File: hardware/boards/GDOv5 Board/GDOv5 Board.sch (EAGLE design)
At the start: 27 parts, among them IC1 DS1820, IC2 3.3V REG, J1 DCJ0202, Q1 BSS84, Q2 BSS138, Q3 BSS138

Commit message: Finalized version of board for OshPark
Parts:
- Q2, Q3: device bss138_10:BSS138 -> Ava:BSS138
- R10, R9: value 50 -> 50Ω
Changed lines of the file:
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@@
 <grid distance="0.1" unitdist="inch" unit="inch" style="lines" multiple="1" display="no" altdistance="0.01" altunitdist="inch" altunit="inch"/>
 <layers>
-<layer number="1" name="Top" color="4" fill="1" visible="no" active="no"/>
-<layer number="16" name="Bottom" color="1" fill="1" visible="no" active="no"/>
-<layer number="17" name="Pads" color="2" fill="1" visible="no" active="no"/>
-<layer number="18" name="Vias" color="2" fill="1" visible="no" active="no"/>
-<layer number="19" name="Unrouted" color="6" fill="1" visible="no" active="no"/>
-<layer number="20" name="Dimension" color="15" fill="1" visible="no" active="no"/>
-<layer number="21" name="tPlace" color="7" fill="1" visible="no" active="no"/>
-<layer number="22" name="bPlace" color="7" fill="1" visible="no" active="no"/>
-<layer number="23" name="tOrigins" color="15" fill="1" visible="no" active="no"/>
-<layer number="24" name="bOrigins" color="15" fill="1" visible="no" active="no"/>
-<layer number="25" name="tNames" color="7" fill="1" visible="no" active="no"/>
-<layer number="26" name="bNames" color="7" fill="1" visible="no" active="no"/>
-<layer number="27" name="tValues" color="7" fill="1" visible="no" active="no"/>
-<layer number="28" name="bValues" color="7" fill="1" visible="no" active="no"/>
+<layer number="1" name="Top" color="4" fill="1" visible="yes" active="no"/>
+<layer number="16" name="Bottom" color="1" fill="1" visible="yes" active="no"/>
+<layer number="17" name="Pads" color="2" fill="1" visible="yes" active="no"/>
+<layer number="18" name="Vias" color="2" fill="1" visible="yes" active="no"/>
+<layer number="19" name="Unrouted" color="6" fill="1" visible="yes" active="no"/>
+<layer number="20" name="Dimension" color="15" fill="1" visible="yes" active="no"/>
+<layer number="21" name="tPlace" color="7" fill="1" visible="yes" active="no"/>
+<layer number="22" name="bPlace" color="7" fill="1" visible="yes" active="no"/>
+<layer number="23" name="tOrigins" color="15" fill="1" visible="yes" active="no"/>
+<layer number="24" name="bOrigins" color="15" fill="1" visible="yes" active="no"/>
+<layer number="25" name="tNames" color="7" fill="1" visible="yes" active="no"/>
+<layer number="26" name="bNames" color="7" fill="1" visible="yes" active="no"/>
+<layer number="27" name="tValues" color="7" fill="1" visible="yes" active="no"/>
+<layer number="28" name="bValues" color="7" fill="1" visible="yes" active="no"/>
 <layer number="29" name="tStop" color="7" fill="3" visible="no" active="no"/>
 <layer number="30" name="bStop" color="7" fill="6" visible="no" active="no"/>
@@
 <layer number="35" name="tGlue" color="7" fill="4" visible="no" active="no"/>
 <layer number="36" name="bGlue" color="7" fill="5" visible="no" active="no"/>
-<layer number="37" name="tTest" color="7" fill="1" visible="no" active="no"/>
-<layer number="38" name="bTest" color="7" fill="1" visible="no" active="no"/>
+<layer number="37" name="tTest" color="7" fill="1" visible="yes" active="no"/>
+<layer number="38" name="bTest" color="7" fill="1" visible="yes" active="no"/>
 <layer number="39" name="tKeepout" color="4" fill="11" visible="no" active="no"/>
 <layer number="40" name="bKeepout" color="1" fill="11" visible="no" active="no"/>
@@
 <layer number="44" name="Drills" color="7" fill="1" visible="no" active="no"/>
 <layer number="45" name="Holes" color="7" fill="1" visible="no" active="no"/>
-<layer number="46" name="Milling" color="3" fill="1" visible="no" active="no"/>
-<layer number="47" name="Measures" color="7" fill="1" visible="no" active="no"/>
-<layer number="48" name="Document" color="7" fill="1" visible="no" active="no"/>
-<layer number="49" name="Reference" color="7" fill="1" visible="no" active="no"/>
-<layer number="50" name="dxf" color="7" fill="1" visible="no" active="no"/>
-<layer number="51" name="tDocu" color="7" fill="1" visible="no" active="no"/>
-<layer number="52" name="bDocu" color="7" fill="1" visible="no" active="no"/>
-<layer number="53" name="tGND_GNDA" color="7" fill="9" visible="no" active="no"/>
-<layer number="54" name="bGND_GNDA" color="1" fill="9" visible="no" active="no"/>
-<layer number="56" name="wert" color="7" fill="1" visible="no" active="no"/>
-<layer number="57" name="tCAD" color="7" fill="1" visible="no" active="no"/>
-<layer number="59" name="tCarbon" color="7" fill="1" visible="no" active="no"/>
-<layer number="60" name="bCarbon" color="7" fill="1" visible="no" active="no"/>
+<layer number="46" name="Milling" color="3" fill="1" visible="yes" active="no"/>
+<layer number="47" name="Measures" color="7" fill="1" visible="yes" active="no"/>
+<layer number="48" name="Document" color="7" fill="1" visible="yes" active="no"/>
+<layer number="49" name="Reference" color="7" fill="1" visible="yes" active="no"/>
+<layer number="50" name="dxf" color="7" fill="1" visible="yes" active="no"/>
+<layer number="51" name="tDocu" color="7" fill="1" visible="yes" active="no"/>
+<layer number="52" name="bDocu" color="7" fill="1" visible="yes" active="no"/>
+<layer number="53" name="tGND_GNDA" color="7" fill="9" visible="yes" active="no"/>
+<layer number="54" name="bGND_GNDA" color="1" fill="9" visible="yes" active="no"/>
+<layer number="56" name="wert" color="7" fill="1" visible="yes" active="no"/>
+<layer number="57" name="tCAD" color="7" fill="1" visible="yes" active="no"/>
+<layer number="59" name="tCarbon" color="7" fill="1" visible="yes" active="no"/>
+<layer number="60" name="bCarbon" color="7" fill="1" visible="yes" active="no"/>
 <layer number="90" name="Modules" color="5" fill="1" visible="yes" active="yes"/>
 <layer number="91" name="Nets" color="2" fill="1" visible="yes" active="yes"/>
@@
 <part name="R5" library="resistor" deviceset="R-EU_" device="M3216" value="250"/>
 <part name="GND12" library="supply1" deviceset="GND" device=""/>
-<part name="R9" library="resistor" deviceset="R-EU_" device="M3216" value="50"/>
+<part name="R9" library="resistor" deviceset="R-EU_" device="M3216" value="50Ω"/>
 <part name="GND5" library="supply1" deviceset="GND" device=""/>
-<part name="R10" library="resistor" deviceset="R-EU_" device="M3216" value="50"/>
+<part name="R10" library="resistor" deviceset="R-EU_" device="M3216" value="50Ω"/>
 <part name="GND13" library="supply1" deviceset="GND" device=""/>
 <part name="C8" library="SparkFun-Capacitors" deviceset="10UF-TANT" device="" value="10uF"/>
@@
 <part name="GND1" library="supply1" deviceset="GND" device=""/>
 <part name="Q1" library="transistor-small-signal" deviceset="BSS84" device=""/>
-<part name="Q2" library="bss138_10" deviceset="BSS138" device=""/>
-<part name="Q3" library="bss138_10" deviceset="BSS138" device=""/>
+<part name="Q2" library="Ava" deviceset="BSS138" device=""/>
+<part name="Q3" library="Ava" deviceset="BSS138" device=""/>
 <part name="R2" library="resistor" deviceset="R-EU_" device="M3216" value="100k"/>
 <part name="R3" library="resistor" deviceset="R-EU_" device="M3216" value="100k"/>

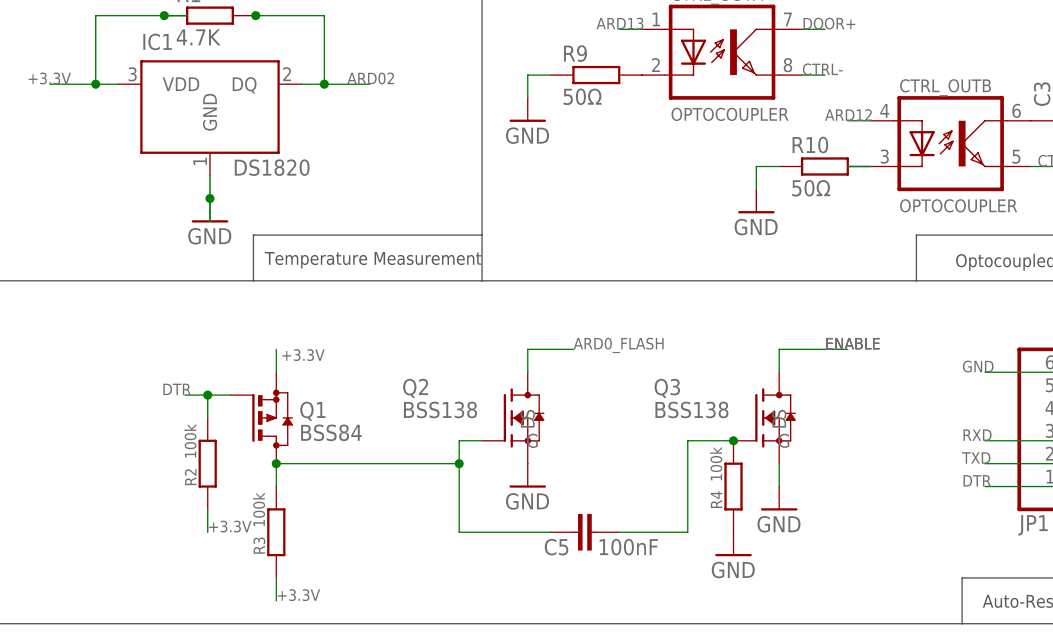
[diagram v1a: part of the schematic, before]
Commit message: Fixing bad pull down connection in auto-reset circuit
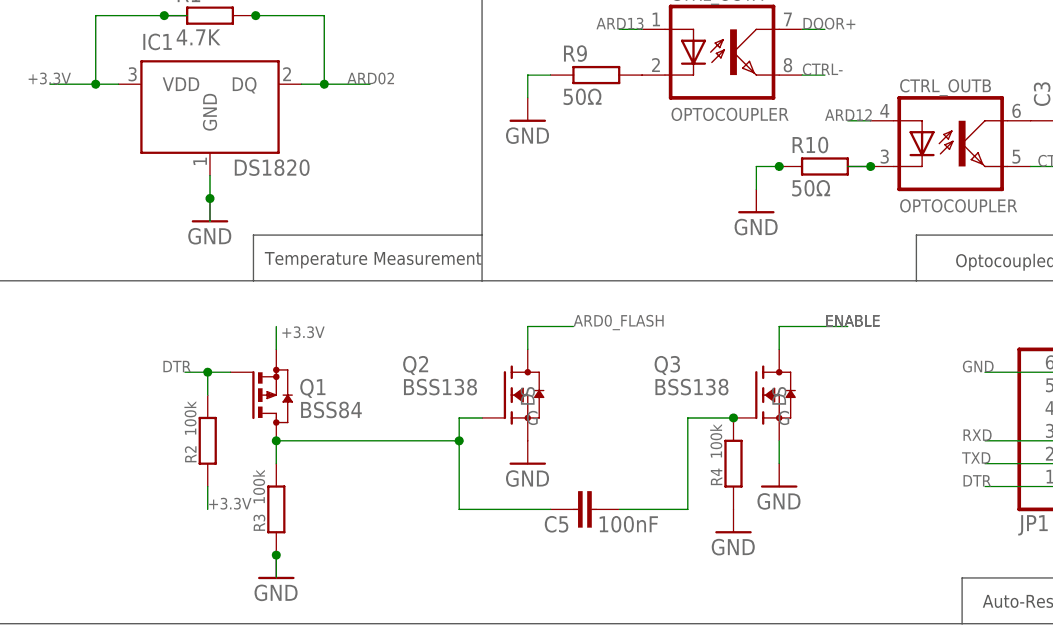
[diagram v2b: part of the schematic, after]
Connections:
- net +3.3V: no longer R3.1
- net GND: now also R3.1
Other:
- moved on the sheet: C5, Q1, Q2, Q3, R2, R3, R4

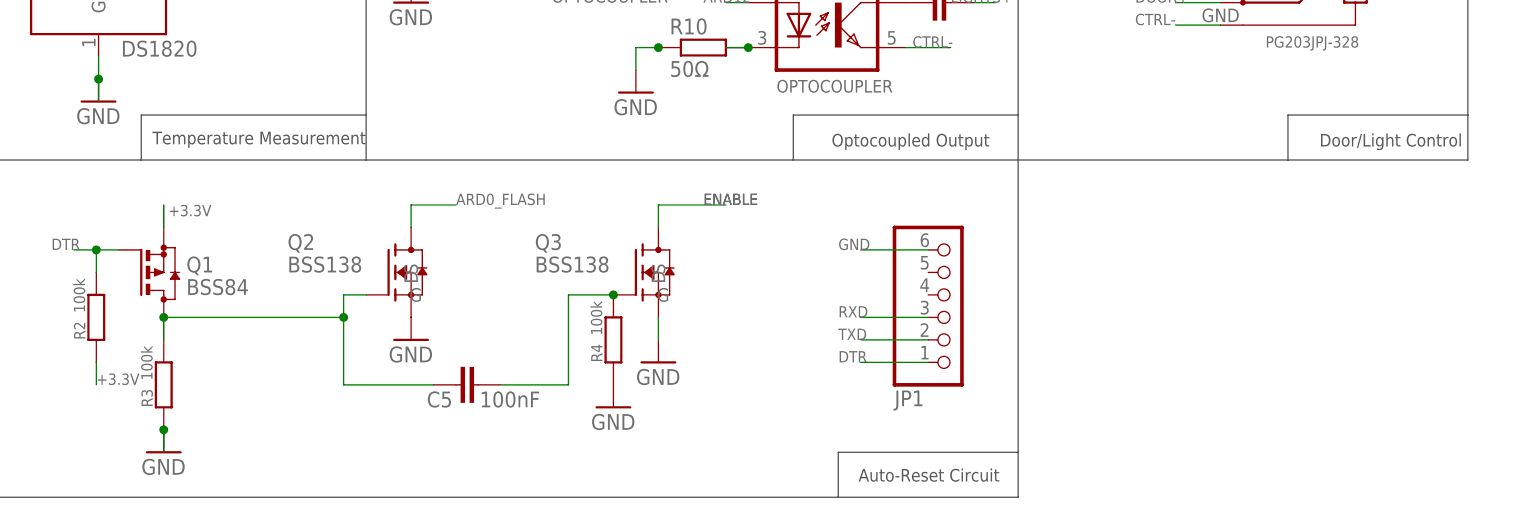
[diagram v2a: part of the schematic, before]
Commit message: Added pullup resistor for GPIO0
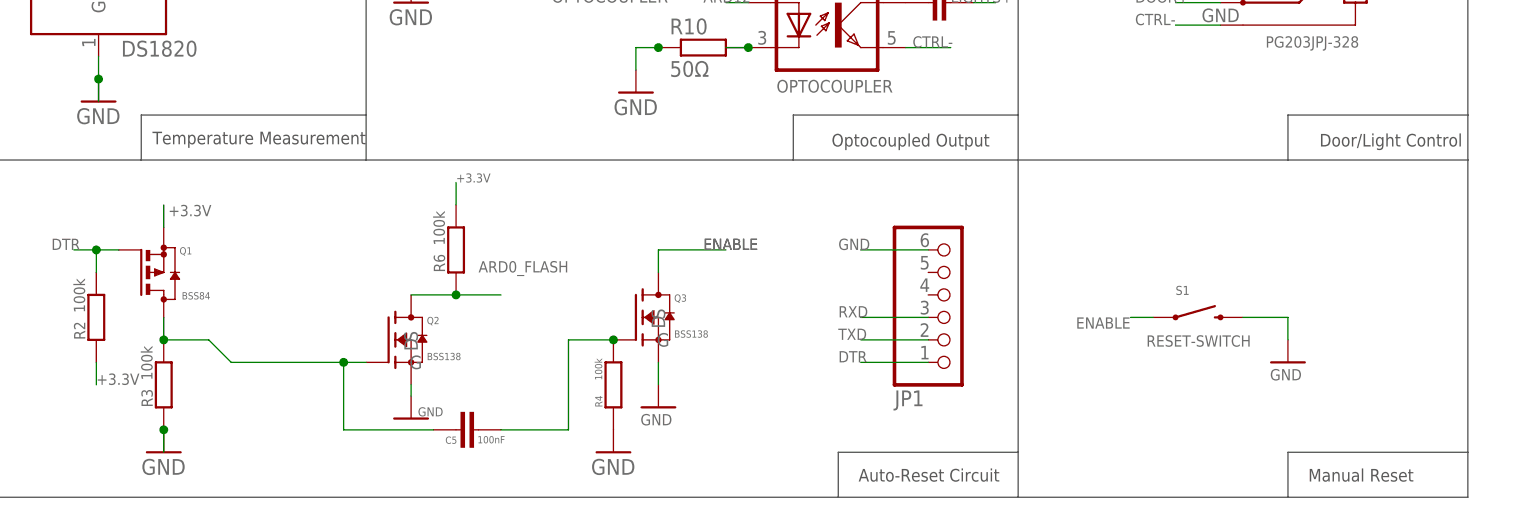
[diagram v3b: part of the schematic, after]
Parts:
- added R6: 100k, resistor:R-EU_M3216
- added S1: RESET-SWITCH, SparkFun-Electromechanical:SWITCH-MOMENTARY-2-SMD-1101NE
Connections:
- net +3.3V: now also R6.2
- net ARD0_FLASH: now also R6.1
- net ENABLE: now also S1.1
- net GND: now also S1.2
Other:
- note added: "Manual Reset"
- moved on the sheet: C5, Q2, Q3, R4

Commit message: Fixing Board issues
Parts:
- added Q4: IRLML2502, bss138_10:BSS138
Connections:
- new net N$1: J1.3, Q4.D
- net +5V: now also J1.1, Q4.G; no longer J1.3
- net GND: now also Q4.S; no longer J1.1
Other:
- moved on the sheet: C4, C8, C9, IC2, J1
